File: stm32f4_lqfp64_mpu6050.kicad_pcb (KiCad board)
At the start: 2 copper layers, 40 x 25 mm, 337 parts, among them M1 ALIS-CUSTOM-PARTS_POWERPADS, M2 ALIS-CUSTOM-PARTS_POWERPADS, M3 ALIS-CUSTOM-PARTS_POWERPADS, M5 ALIS-CUSTOM-PARTS_POWERPADS, Q1 BSS138, Q2 BSS138, Q3 BSS138, Q5 BSS138, U1 STM32F405R, U2 MPU6050, U3 LP2985LV, U4 LP2985LV, U5 TPS63002, U6 LMH1980, U7 TS5A3160, U8 TS5A3160, U9 LT6206, X3 CRYSTAL_SMD

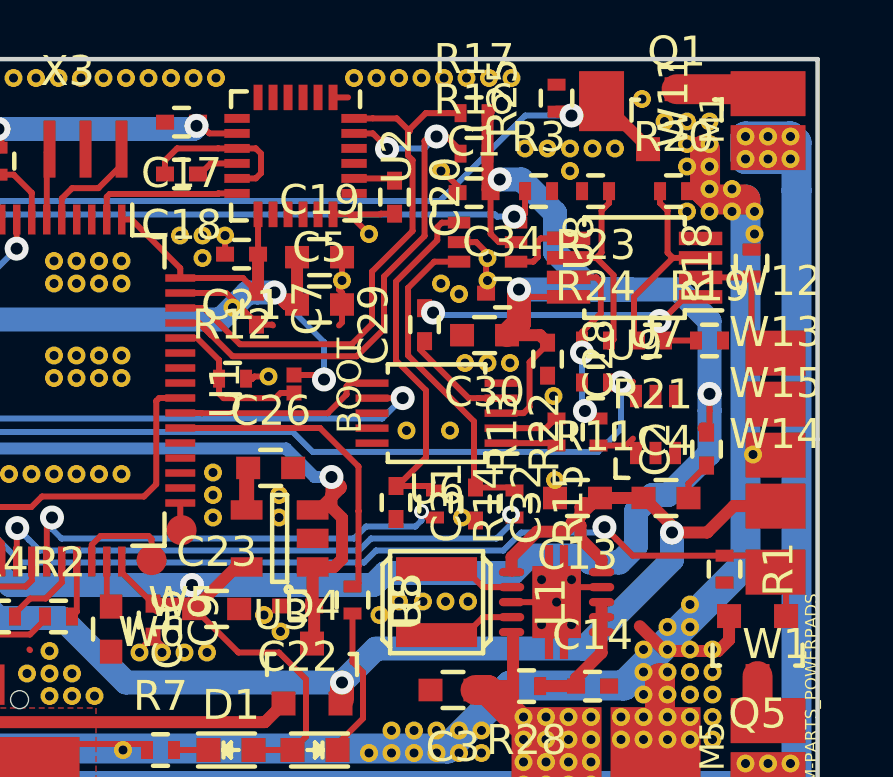
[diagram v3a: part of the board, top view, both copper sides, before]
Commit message: fixed video opamp and output switch circuit, removed line termination resistors
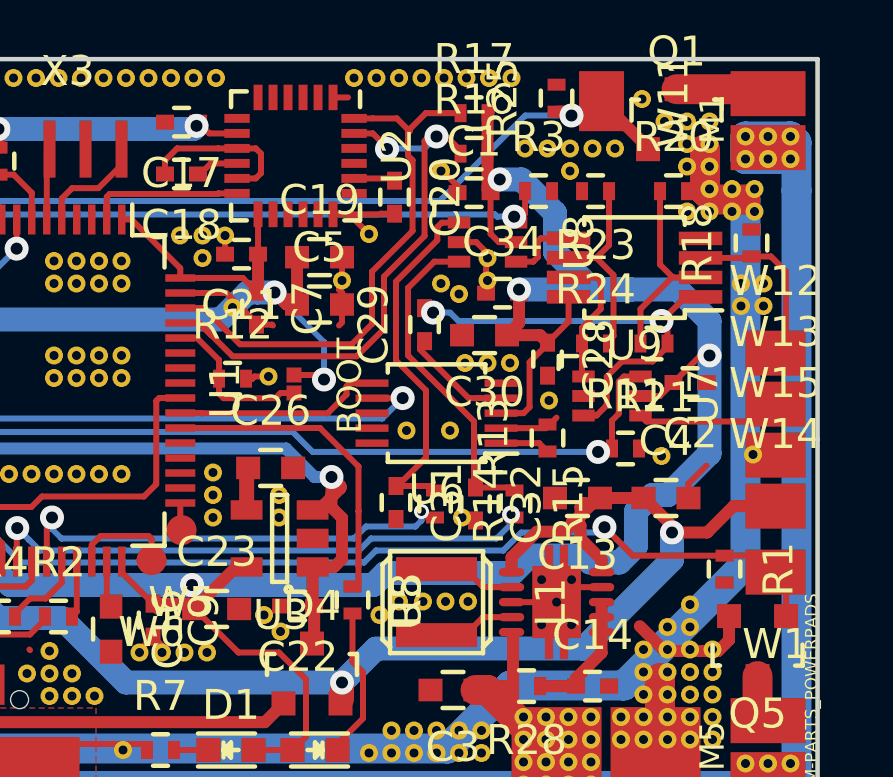
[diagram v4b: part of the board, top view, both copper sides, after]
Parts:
- removed the ? at (129.3, 103.7)
- removed the ? at (129.4, 106.5)
- removed R19, R22: 75R, Resistors_SMD:R_0402
- added ?: , alis_parts:via_04_no_front_mask, F.Cu at (136.3, 100.7)
- added ?: , alis_parts:via_04_no_front_mask, F.Cu at (135.6, 100.7)
- added ?: , alis_parts:via_04_no_front_mask, F.Cu at (135.6, 100.0)
- added ?: , alis_parts:via_04_no_front_mask, F.Cu at (136.3, 100.0)
- added ?: , alis_parts:via_04_no_front_mask, F.Cu at (132.9, 105.7)
- added ?: , alis_parts:via_04_no_front_mask, F.Cu at (129.2, 103.9)
- R18: value 75R -> NP!
- R20, R23: value 490R -> NP!
- R21, R24: value 490R -> 0R
- moved R11 2.42 mm to (131.7, 105.5), turned to 0 degrees
- moved C2 2.29 mm to (133.9, 103.3), turned to 180 degrees
- moved U7 1.73 mm to (131.3, 103.7), turned to 270 degrees
- moved ? 0.75 mm to (136.0, 97.6)
- moved ? 0.75 mm to (136.0, 96.8)
- moved R18 0.67 mm to (135.9, 98.6)
- moved R13 0.36 mm to (129.1, 105.1)
- moved R21 0.11 mm to (132.7, 102.0)
- moved R24 0.10 mm to (130.7, 102.0)
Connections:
- U7 pad 1: Net-(R22-Pad1) -> bw_buffered
- U7 pad 3: Net-(R19-Pad2) -> video_buffered
- U9 pad 2: VIDEO_IN -> Net-(R20-Pad1)
- U9 pad 3: Net-(R20-Pad1) -> VIDEO_IN
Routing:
- net VIDEO_OUT: track 0.00 -> 4.82 mm
- net video_buffered: track 11.7 -> 15.1 mm
- net VIDEO_IN: track 3.90 -> 5.94 mm
- net bw_buffered: track 6.52 -> 4.57 mm, vias 2 -> 0
- net Net-(R22-Pad1): track 1.24 -> 0.00 mm
- net BW_MASK: track 30.8 -> 31.4 mm

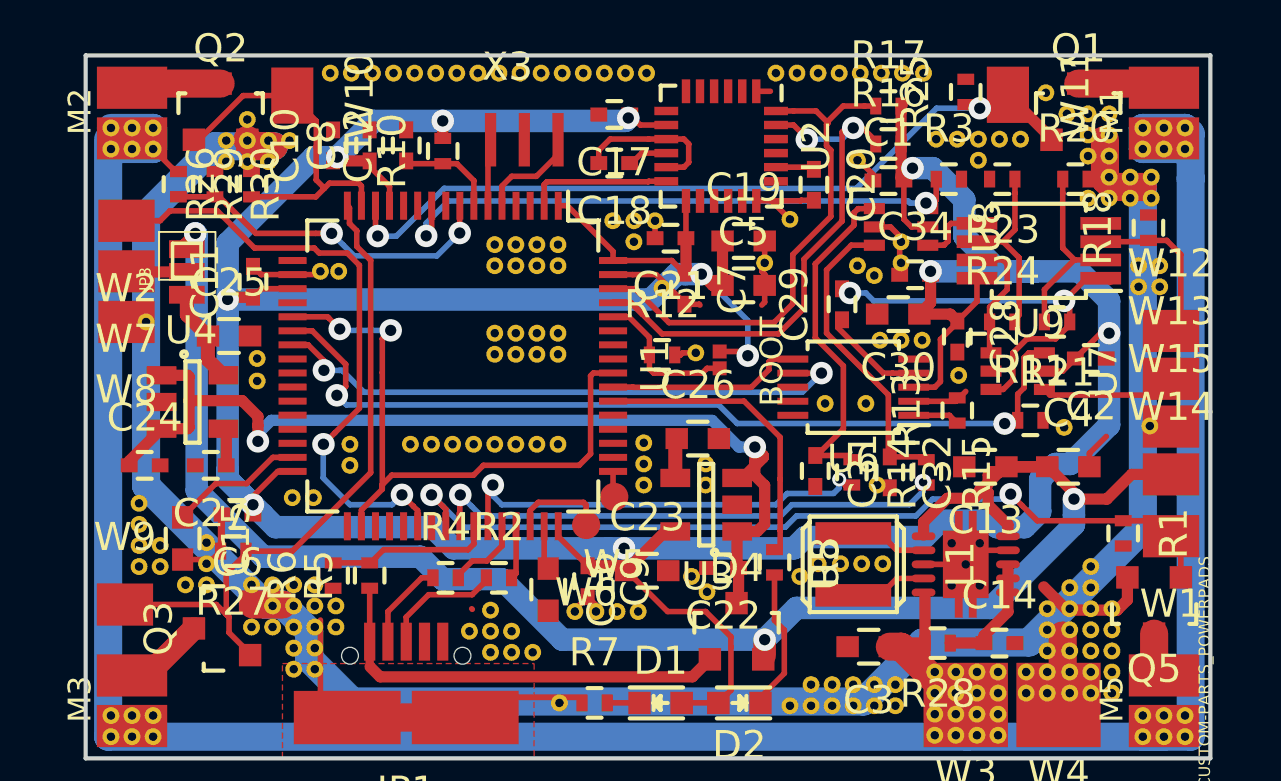
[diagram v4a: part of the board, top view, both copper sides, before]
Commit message: fixed opamp circuit and some cosmetics
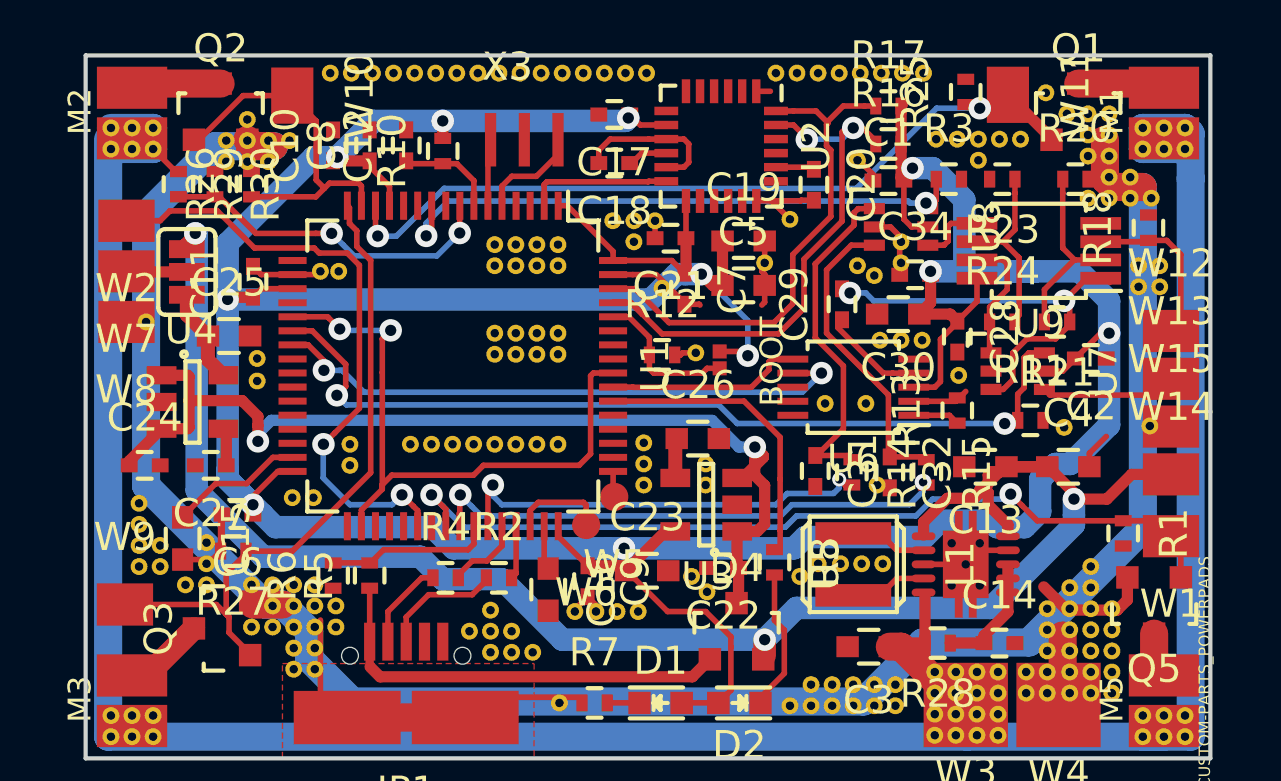
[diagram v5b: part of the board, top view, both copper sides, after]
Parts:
- removed the ? at (136.0, 96.8)
- JP3: footprint minimal:SPARKFUN-PASSIVES_PAD-JUMPER-3-2OF3_NC_BY_PASTE_YES_SILK_FULL_BOX -> SPARKFUN-PASSIVES_PAD-JUMPER-3-2OF3_NC_BY_PASTE_YES_SILK_FULL_BOX
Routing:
- net 3.3V: track 154.8 -> 155.6 mm
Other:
- board text added: "Monkeybrain v0.1.1 Alexander Tuxen 09/2016"
- board text removed: "Monkeybrain v0.1 © Alexander Tuxen 2016"
